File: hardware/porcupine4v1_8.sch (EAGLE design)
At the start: 33 parts, among them X1 PROGCON

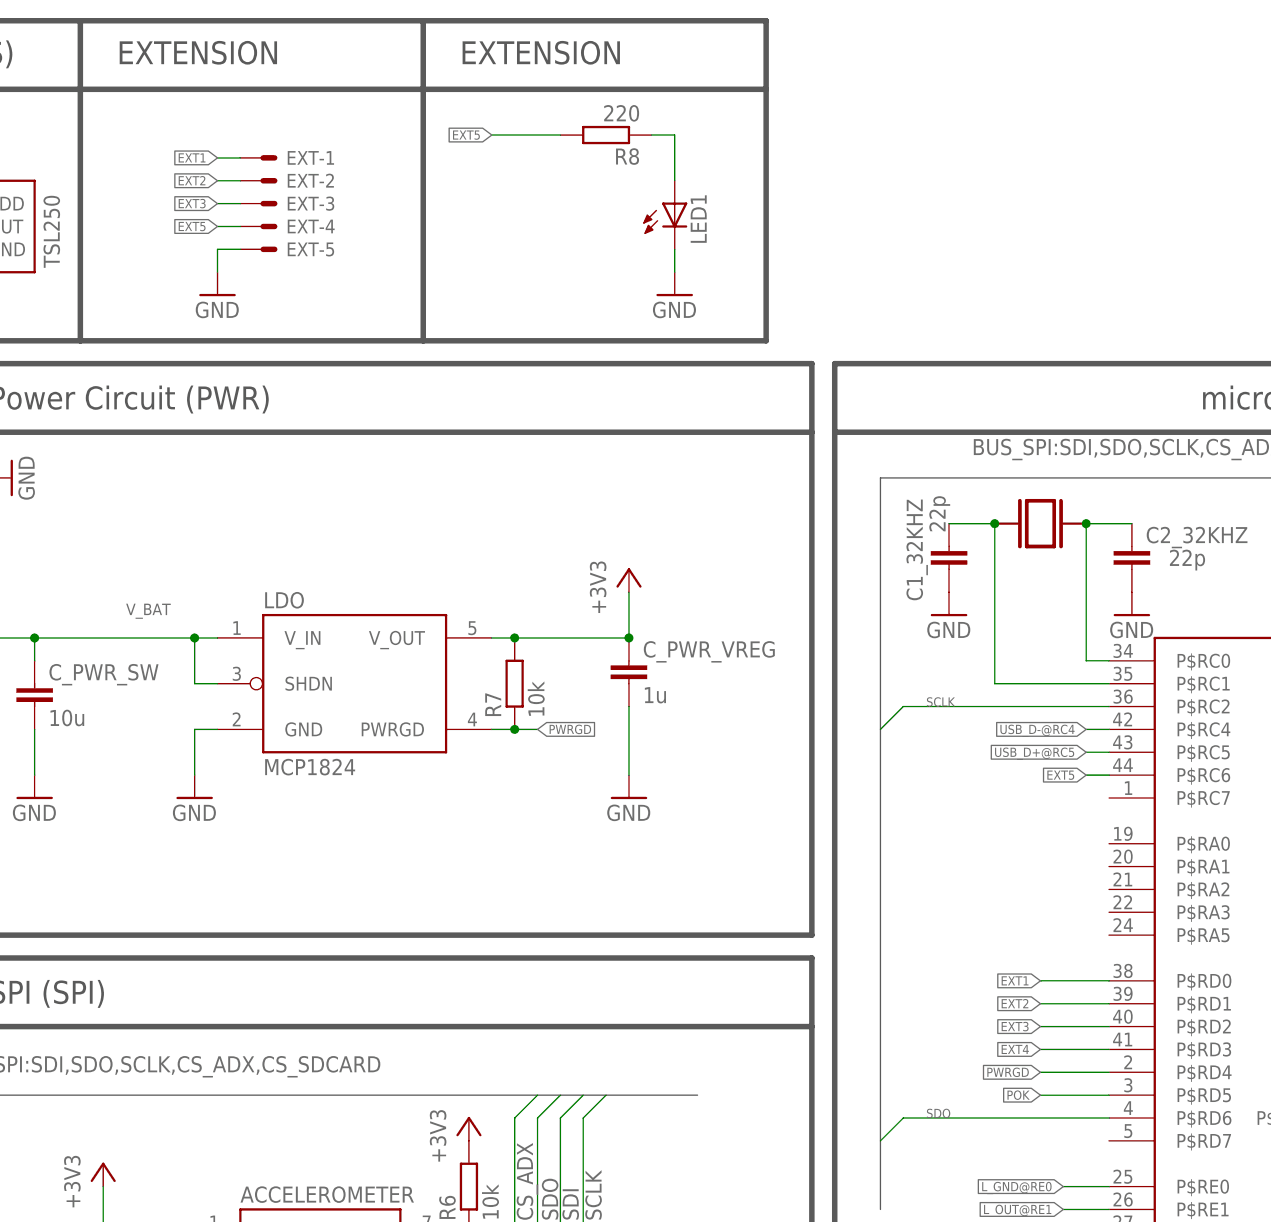
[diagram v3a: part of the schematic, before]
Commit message: porcupine4v1_8: updated extension pins (names), shifted some vias
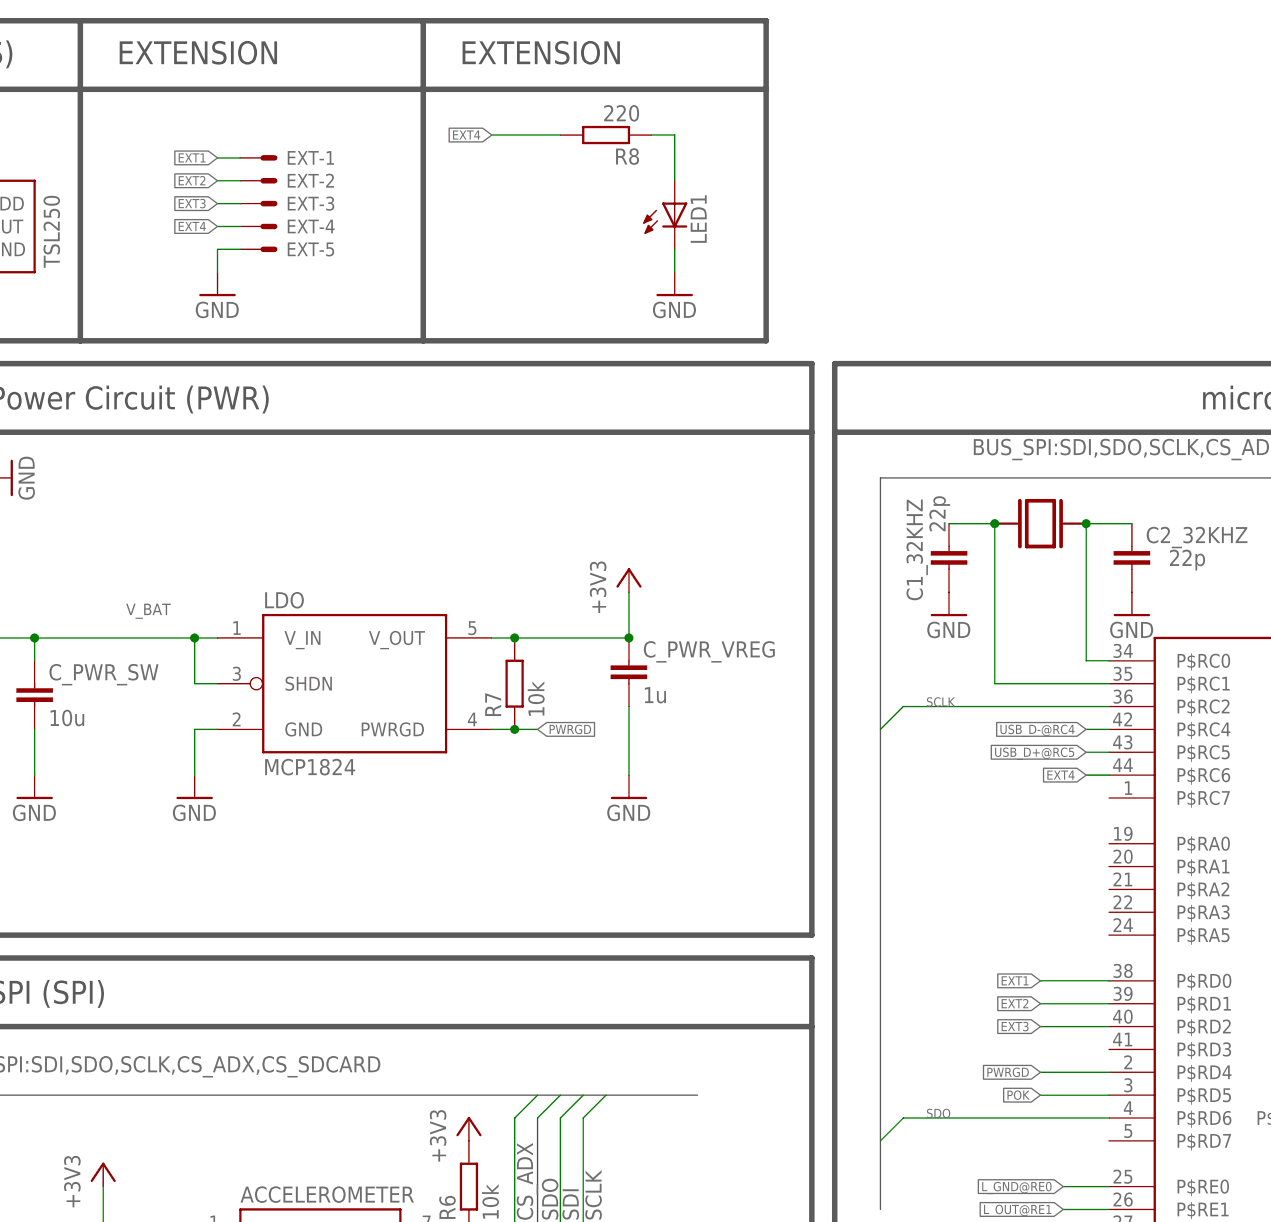
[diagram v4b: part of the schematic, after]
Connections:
- removed net EXT5: EXT-4.S, PIC_CONTROLLER.P$RC6, R8.2
- net EXT4: now also EXT-4.S, PIC_CONTROLLER.P$RC6, R8.2; no longer PIC_CONTROLLER.P$RD3
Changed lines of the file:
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@@
-</segment>
-</net>
-<net name="EXT4" class="0">
-<segment>
-<pinref part="PIC_CONTROLLER" gate="G$1" pin="P$RD3"/>
-<wire x1="208.28" y1="53.34" x2="200.66" y2="53.34" width="0.1524" layer="91"/>
-<label x="200.66" y="53.34" size="1.016" layer="95" rot="R180" xref="yes"/>
-</segment>
-</net>
-<net name="EXT5" class="0">
-<segment>
-<wire x1="111.76" y1="144.78" x2="109.22" y2="144.78" width="0.1524" layer="91"/>
-<label x="109.22" y="144.78" size="1.016" layer="95" rot="R180" xref="yes"/>
-<pinref part="EXT" gate="-4" pin="S"/>
-</segment>
-<segment>
-<pinref part="PIC_CONTROLLER" gate="G$1" pin="P$RC6"/>
-<wire x1="208.28" y1="83.82" x2="205.74" y2="83.82" width="0.1524" layer="91"/>
-<label x="205.74" y="83.82" size="1.016" layer="95" rot="R180" xref="yes"/>
-</segment>
-<segment>
-<wire x1="147.32" y1="154.94" x2="139.7" y2="154.94" width="0.1524" layer="91"/>
-<label x="139.7" y="154.94" size="1.016" layer="95" rot="R180" xref="yes"/>
-<pinref part="R8" gate="G$1" pin="2"/>
 </segment>
 </net>
@@
 </segment>
 </net>
+<net name="EXT4" class="0">
+<segment>
+<pinref part="PIC_CONTROLLER" gate="G$1" pin="P$RC6"/>
+<wire x1="208.28" y1="83.82" x2="205.74" y2="83.82" width="0.1524" layer="91"/>
+<label x="205.74" y="83.82" size="1.016" layer="95" rot="R180" xref="yes"/>
+</segment>
+<segment>
+<wire x1="111.76" y1="144.78" x2="109.22" y2="144.78" width="0.1524" layer="91"/>
+<label x="109.22" y="144.78" size="1.016" layer="95" rot="R180" xref="yes"/>
+<pinref part="EXT" gate="-4" pin="S"/>
+</segment>
+<segment>
+<wire x1="147.32" y1="154.94" x2="139.7" y2="154.94" width="0.1524" layer="91"/>
+<label x="139.7" y="154.94" size="1.016" layer="95" rot="R180" xref="yes"/>
+<pinref part="R8" gate="G$1" pin="2"/>
+</segment>
+</net>
